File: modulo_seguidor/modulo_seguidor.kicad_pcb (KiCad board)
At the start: 2 copper layers, 150 x 76 mm, 30 parts, among them J1 Battery, J2 Motor A Entradas, J3 Motor B Entradas, J4 Motor A Salidas, J5 Motor B Salidas, J6 puerto sensores, M1 Motor_IZQ, M2 Motor_DER, SW1 SW_Push, SW2 SW_Nidec_CAS-120A1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

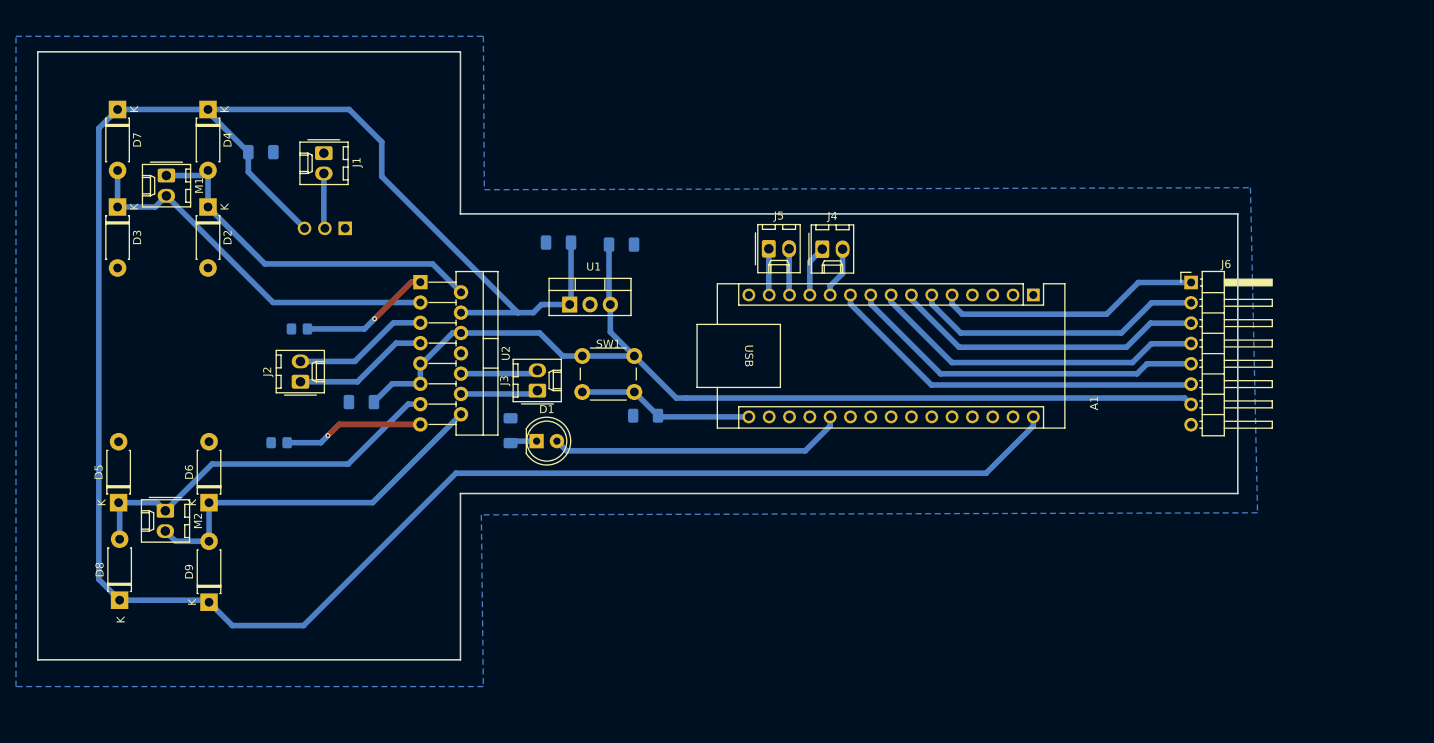
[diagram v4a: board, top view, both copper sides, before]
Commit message: Cambio de pistas
el sector de GND del puente H quedaba aislado. Moví un par de cosas para asegurar que todo GND esté conectado
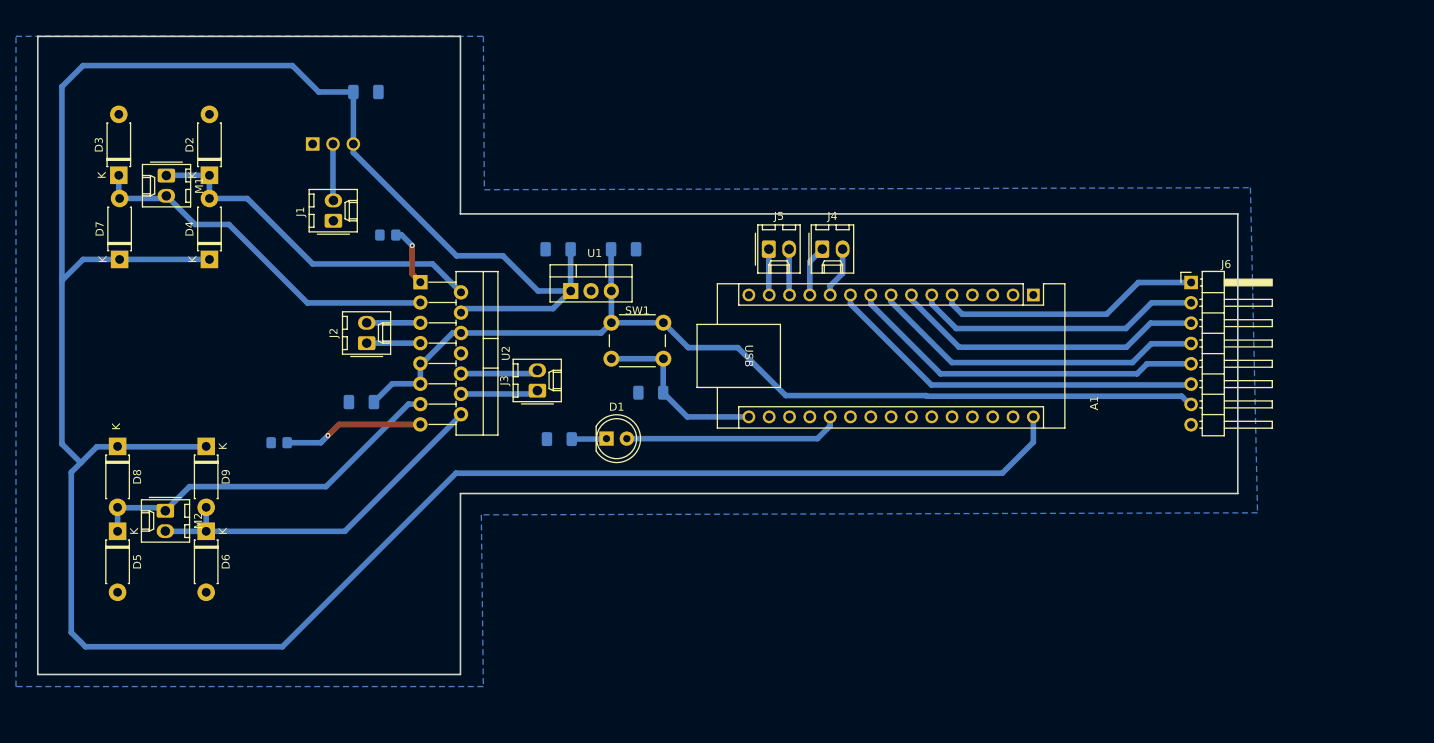
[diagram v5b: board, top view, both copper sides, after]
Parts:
- moved D9 19.5 mm to (87.3, 112.2), turned to -90 degrees
- moved D8 19.2 mm to (76.2, 112.2), turned to -90 degrees
- moved D7 18.7 mm to (76.5, 88.8), turned to 90 degrees
- moved D4 18.7 mm to (87.7, 88.8), turned to 90 degrees
- moved R3 16.1 mm to (110.0, 85.8)
- moved C1 15.1 mm to (107.2, 67.9)
- moved SW2 11.3 mm to (100.6, 74.4), turned to -90 degrees
- moved J2 9.58 mm to (107.3, 99.3)
- moved D1 8.74 mm to (137.3, 111.3)
- moved J1 8.54 mm to (103.2, 84.0), turned to 90 degrees
- moved R2 6.19 mm to (131.4, 111.3), turned to 180 degrees
- moved SW1 5.53 mm to (137.9, 96.8)
- moved D2 3.97 mm to (87.7, 78.3), turned to 90 degrees
- moved D3 3.97 mm to (76.4, 78.3), turned to 90 degrees
- moved D6 3.60 mm to (87.3, 122.8), turned to -90 degrees
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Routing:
- net VCC: track 295.3 -> 341.4 mm
- net Net-(J2-Pin_1): track 17.0 -> 6.71 mm
- net Net-(J2-Pin_2): track 17.0 -> 6.71 mm
- net Net-(A1-A1): track 37.1 -> 27.2 mm
- net Net-(U2-SENSE_A): track 16.5 -> 7.59 mm
- net Salida Regulador: track 126.1 -> 121.2 mm
- net Net-(D3-K): track 48.7 -> 46.2 mm
- net Net-(D5-K): track 48.5 -> 46.9 mm
- net Net-(D2-K): track 46.1 -> 44.6 mm
- net GND: track 1.25 -> 0.00 mm
- net Net-(D1-K): track 3.36 -> 4.36 mm
- net Net-(D6-K): track 46.9 -> 46.1 mm
- net /Boton_encendido: track 22.1 -> 22.8 mm
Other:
- board size 150 x 76 mm -> 150 x 79.8 mm

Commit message: Tamaño de pads
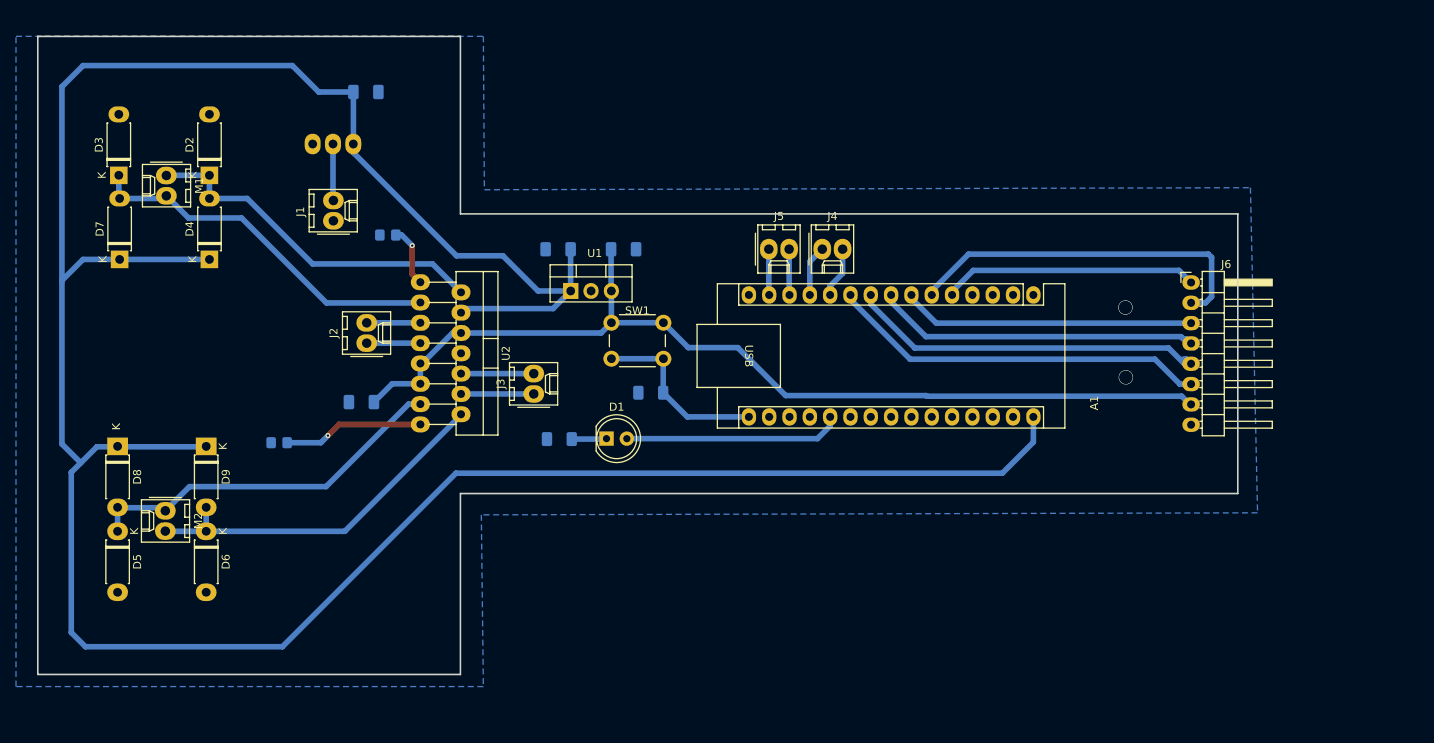
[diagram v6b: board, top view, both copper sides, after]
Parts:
- moved J3 0.62 mm to (128.2, 105.7)
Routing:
- net /Sensor2: track 36.1 -> 45.4 mm
- net /Sensor3: track 39.2 -> 37.2 mm
- net /Sensor4: track 42.4 -> 40.5 mm
- net /Sensor1: track 33.2 -> 32.0 mm
- net /Sensor6: track 48.4 -> 47.4 mm
- net (no net): vias 0 -> 2

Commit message: refactor!(modulo-seguidor): Actualizo la pcb con los cambios del esquemático
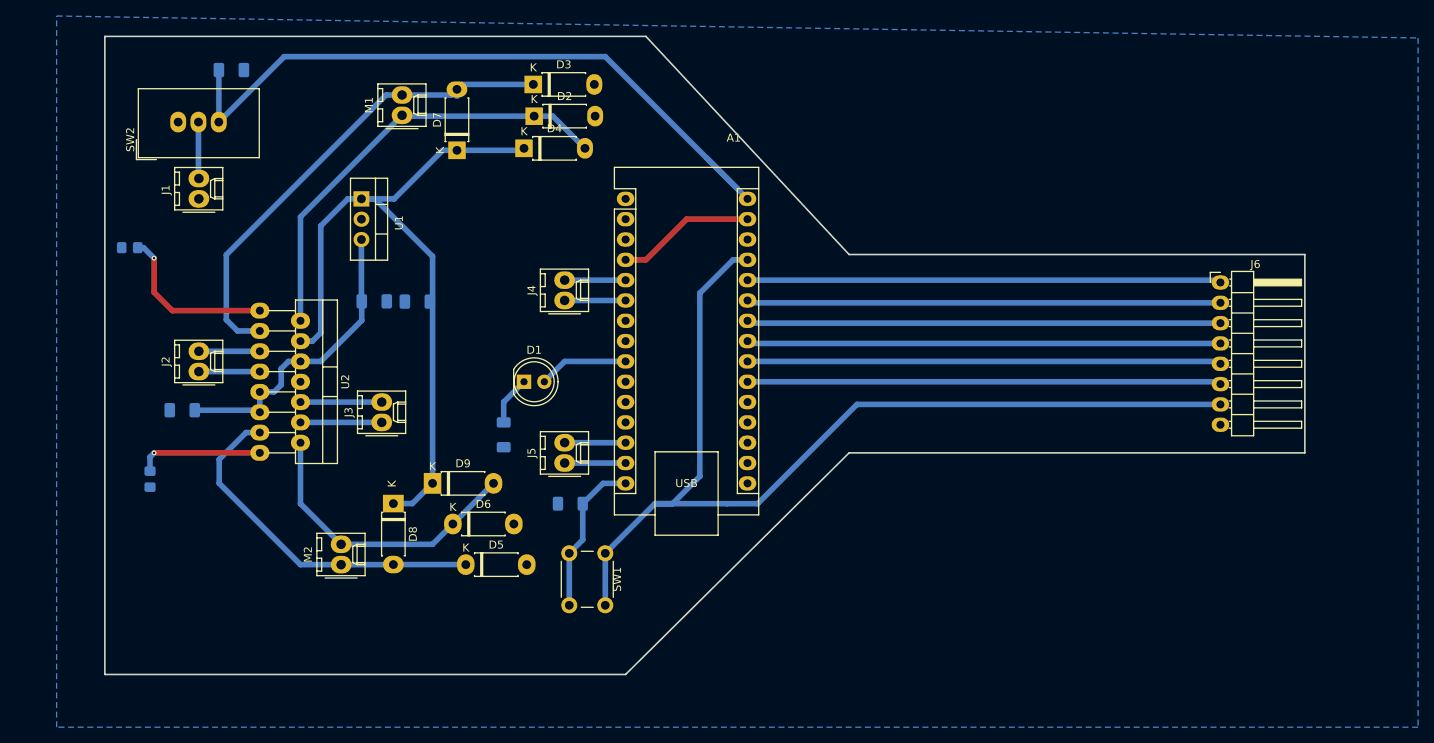
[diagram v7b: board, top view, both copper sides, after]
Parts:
- J4: value Motor A Salidas -> Motor IZQ Arduino OUTPUT
- J5: value Motor B Salidas -> Motor DER Arduino OUTPUT
- SW2: moved to F.Cu
- moved D3 53.0 mm to (128.2, 67.0), turned to 0 degrees
- moved A1 52.4 mm to (139.7, 81.3), turned to 0 degrees
- moved D7 44.3 mm to (118.6, 75.2)
- moved D5 43.7 mm to (119.7, 127.0), turned to 0 degrees
- moved D4 41.7 mm to (127.0, 75.0), turned to 0 degrees
- moved D2 41.3 mm to (128.3, 70.9), turned to 0 degrees
- moved J5 37.0 mm to (132.1, 114.3), turned to 90 degrees
- moved D8 35.2 mm to (110.7, 119.4)
- moved J4 32.8 mm to (132.1, 94.0), turned to 90 degrees
- moved R3 32.3 mm to (77.7, 87.4)
- moved C2 31.8 mm to (108.3, 94.1)
- moved D6 30.8 mm to (118.1, 121.9), turned to 0 degrees
- moved M1 30.4 mm to (111.8, 70.8), turned to 90 degrees
- moved SW1 28.8 mm to (137.2, 125.6), turned to -90 degrees
- moved D9 28.7 mm to (115.6, 116.8), turned to 0 degrees
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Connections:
- A1 pad 10: /Sensor6 -> unconnected-(A1-D7-Pad10)
- A1 pad 11: Net-(A1-D8) -> unconnected-(A1-D8-Pad11)
- A1 pad 12: Net-(A1-D9) -> unconnected-(A1-D9-Pad12)
- A1 pad 15: unconnected-(A1-D12-Pad15) -> /Boton_encendido
- A1 pad 16: /Boton_encendido -> unconnected-(A1-D13-Pad16)
- A1 pad 20: Net-(A1-A1) -> unconnected-(A1-A1-Pad20)
- A1 pad 21: unconnected-(A1-A2-Pad21) -> /Sensor6
- A1 pad 22: unconnected-(A1-A3-Pad22) -> /Sensor5
- A1 pad 23: unconnected-(A1-A4-Pad23) -> /Sensor4
- A1 pad 24: unconnected-(A1-A5-Pad24) -> /Sensor3
- A1 pad 25: unconnected-(A1-A6-Pad25) -> /Sensor2
- A1 pad 26: unconnected-(A1-A7-Pad26) -> /Sensor1
- A1 pad 27: unconnected-(A1-+5V-Pad27) -> +5V
- A1 pad 5: /Sensor1 -> Net-(A1-D2)
- A1 pad 6: /Sensor2 -> Net-(A1-D3)
- A1 pad 7: /Sensor3 -> unconnected-(A1-D4-Pad7)
- A1 pad 8: /Sensor4 -> unconnected-(A1-D5-Pad8)
- A1 pad 9: /Sensor5 -> Net-(A1-D6)
- D1 pad 2: Net-(A1-A1) -> Net-(A1-D6)
- J4 pad 1: Net-(A1-D9) -> Net-(A1-D3)
- J4 pad 2: Net-(A1-D8) -> Net-(A1-D2)
- J6 pad 7: Salida Regulador -> +5V
- R2 pad 1: Net-(D1-K) -> GND
- R2 pad 2: GND -> Net-(D1-K)
- SW1 pad 1: Salida Regulador -> +5V
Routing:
- net VCC: track 341.4 -> 180.7 mm
- net +5V: track 0.00 -> 128.7 mm
- net Salida Regulador: track 121.2 -> 38.4 mm
- net /Sensor1: track 32.0 -> 59.2 mm
- net Net-(A1-A1): track 27.2 -> 0.00 mm
- net /Sensor3: track 37.2 -> 59.2 mm
- net /Sensor4: track 40.5 -> 59.2 mm
- net GND: track 0.00 -> 17.3 mm
- net Net-(D3-K): track 46.2 -> 60.9 mm
- net /Sensor2: track 45.4 -> 59.2 mm
- net /Sensor5: track 45.5 -> 59.2 mm
- net Net-(U2-SENSE_A): track 7.59 -> 21.0 mm
- net /Sensor6: track 47.4 -> 59.2 mm
- net Net-(D2-K): track 44.6 -> 56.0 mm
- net Net-(A1-D6): track 0.00 -> 11.2 mm
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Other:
- outline, holes or cut-outs redrawn

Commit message: refactor(modulo-seguidor): Acomodo componentes de la batería, y pin de 5v del sensor
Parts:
- moved C1 8.97 mm to (99.1, 67.6), turned to -90 degrees
- moved D5 6.40 mm to (113.8, 129.5)
- moved SW2 5.64 mm to (83.8, 66.0)
- moved J1 5.08 mm to (86.2, 76.2)
- moved D6 3.59 mm to (115.6, 124.5)
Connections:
- A1 pad 10: unconnected-(A1-D7-Pad10) -> Net-(A1-D7)
- A1 pad 9: Net-(A1-D6) -> unconnected-(A1-D6-Pad9)
- D1 pad 2: Net-(A1-D6) -> Net-(A1-D7)
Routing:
- net VCC: track 180.7 -> 202.3 mm
- net Net-(A1-D6): track 11.2 -> 0.00 mm
- net Net-(A1-D7): track 0.00 -> 10.2 mm
- net +5V: track 128.7 -> 134.3 mm
- net Net-(D5-K): track 44.5 -> 39.7 mm
- net Net-(D6-K): track 37.0 -> 35.7 mm
- net Net-(J1-Pin_2): track 7.01 -> 7.70 mm
